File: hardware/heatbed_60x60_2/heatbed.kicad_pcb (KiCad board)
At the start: 2 copper layers, 60 x 60 mm, 1 part, among them J1 PWR

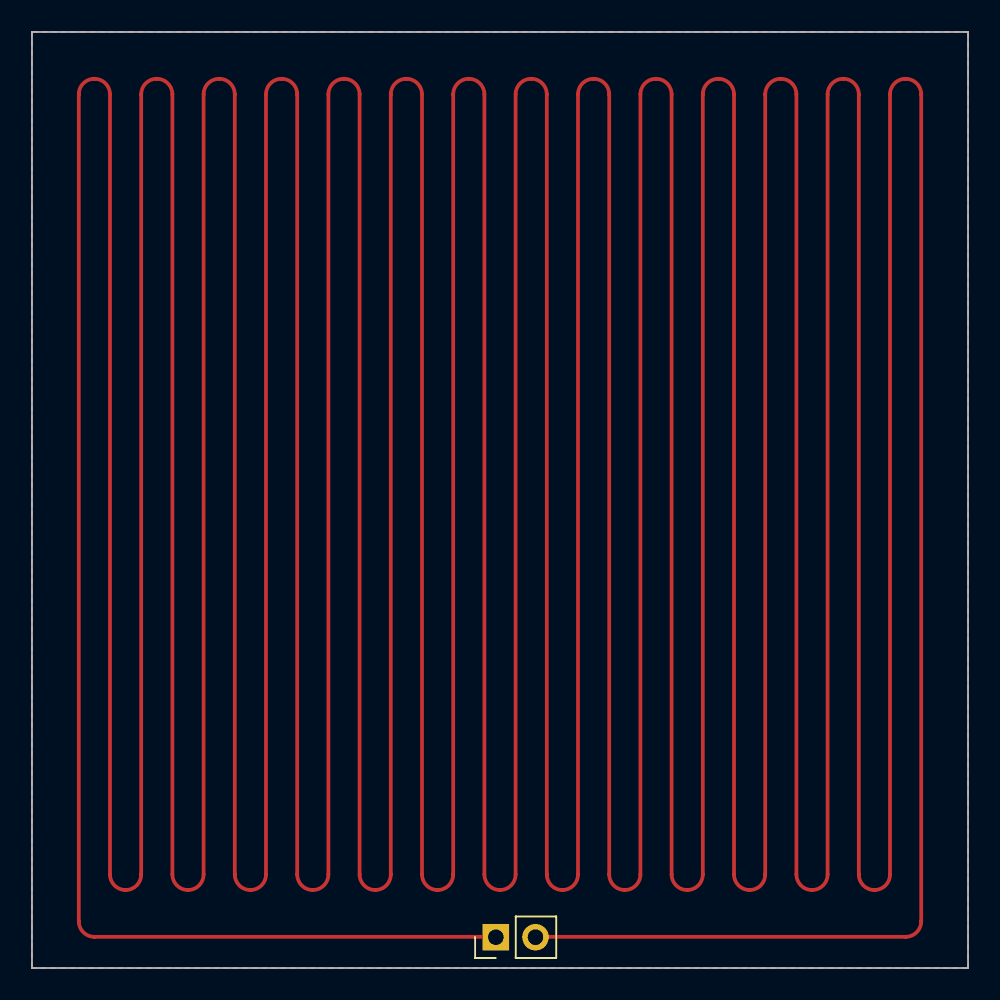
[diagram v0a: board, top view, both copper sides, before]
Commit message: Further increase tracks' widths
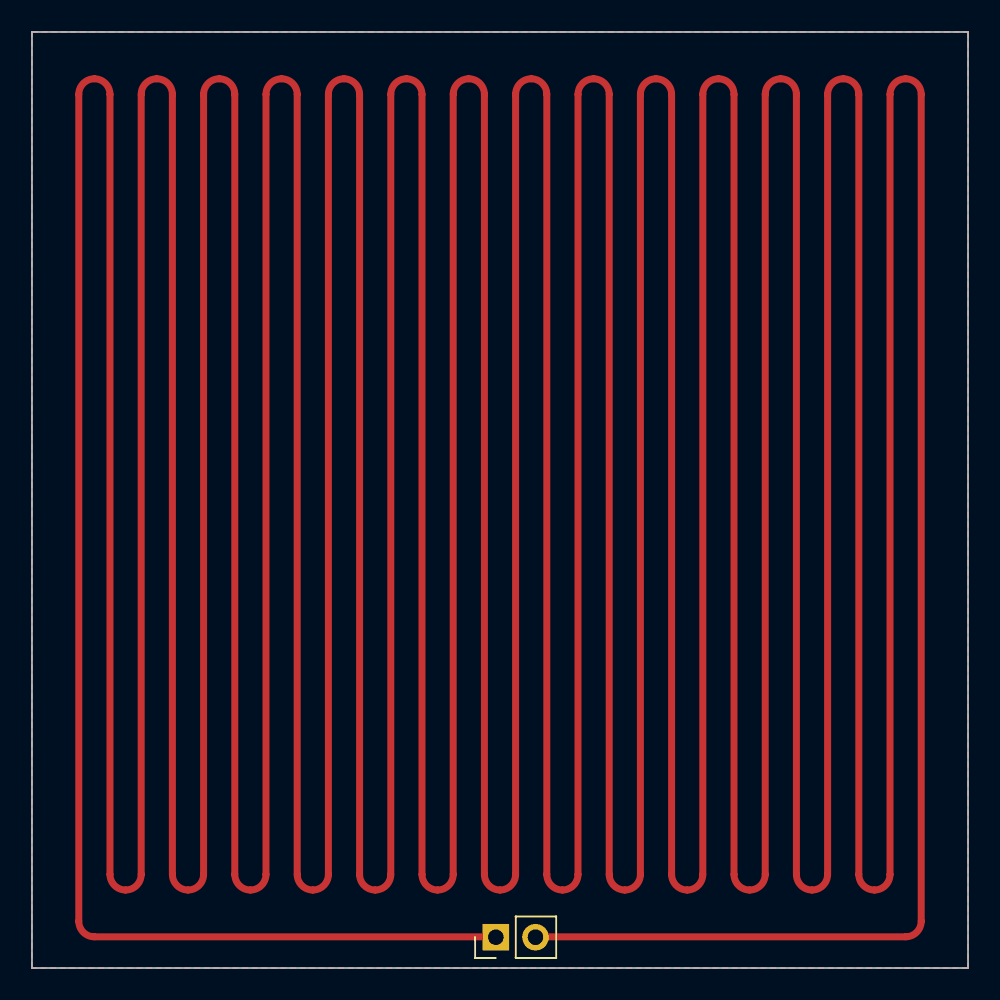
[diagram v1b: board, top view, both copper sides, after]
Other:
- board text added: "Width: 0.449 mm | Length: 1543.49 mm | Resistance: 2.97 Ω"
- board text removed: "Width: 0.241 mm | Length: 1543.49 mm | Resistance: 5.24 Ω"

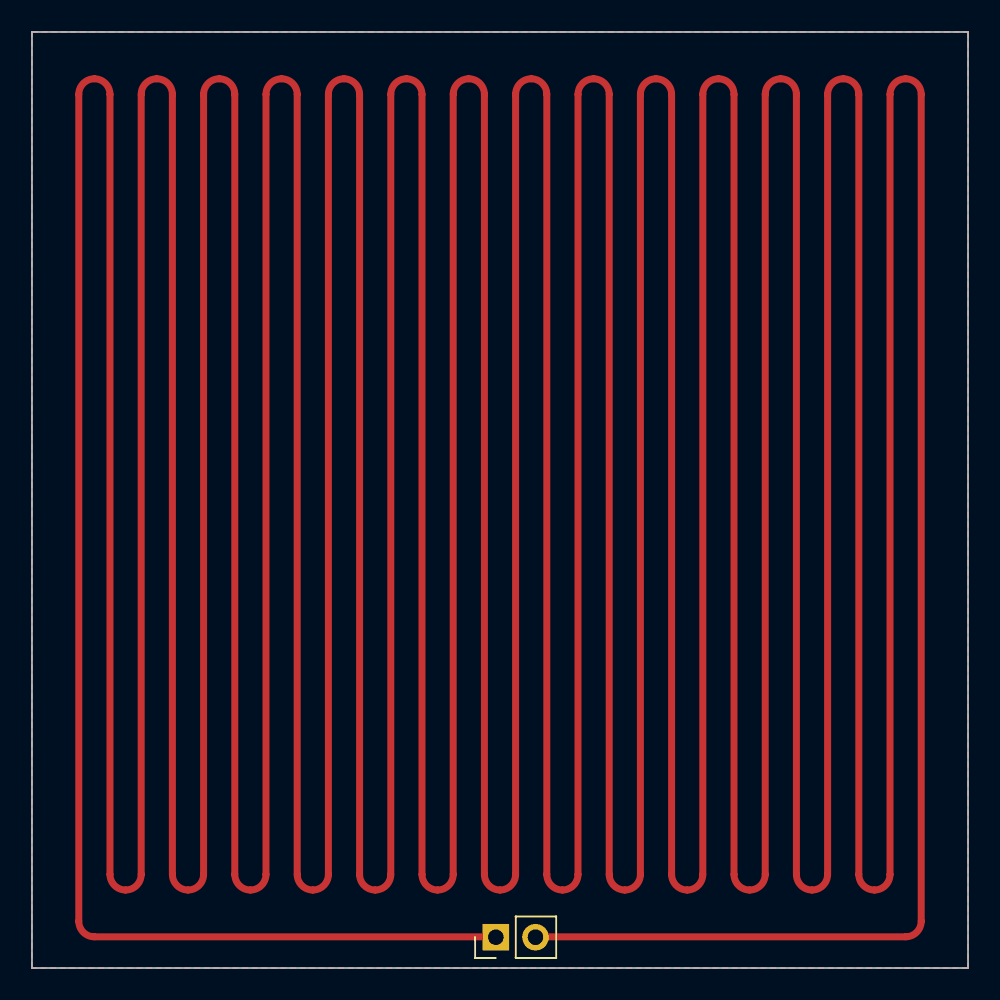
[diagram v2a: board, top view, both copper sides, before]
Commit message: Increase holes' diameters
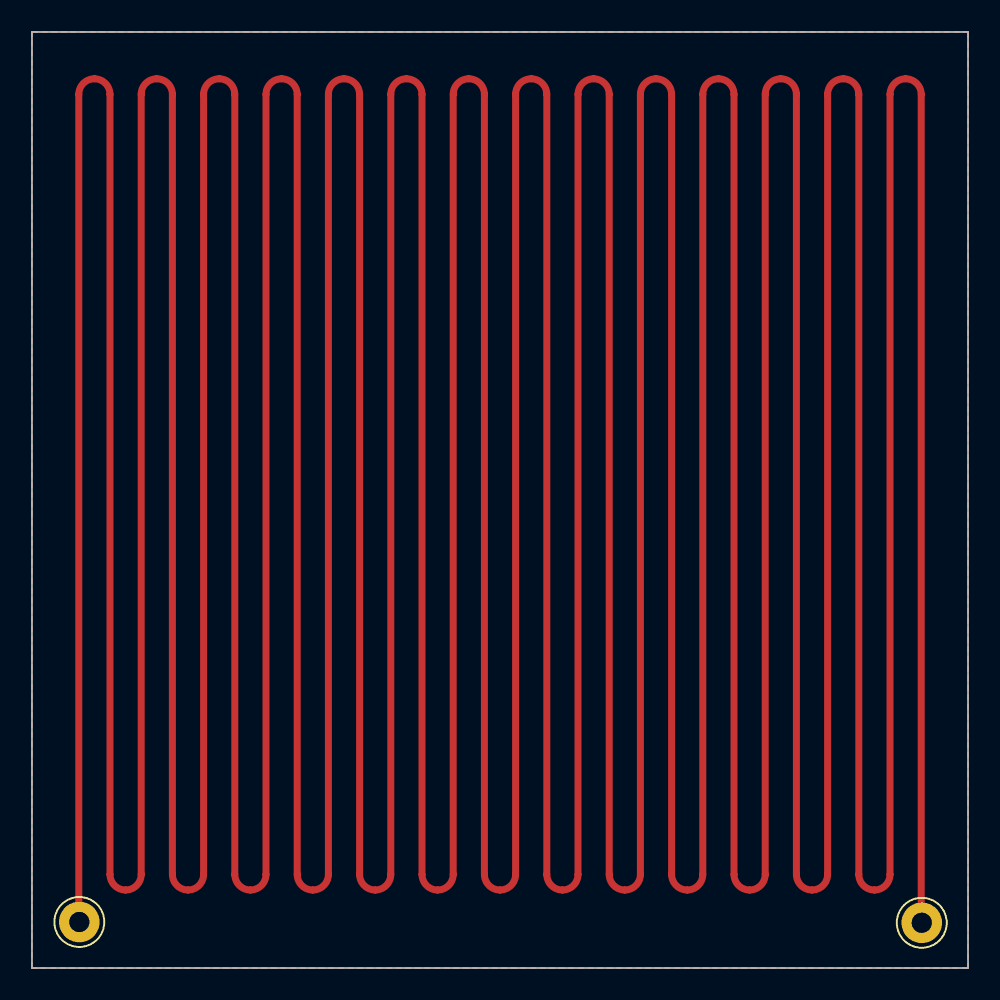
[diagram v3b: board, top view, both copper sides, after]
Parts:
- added J2: Conn_01x01, Connector_Pin:Pin_D1.3mm_L11.0mm, F.Cu at (176.0, 130.1)
- J1: value PWR -> Conn_01x01; footprint Connector_PinHeader_2.54mm:PinHeader_1x02_P2.54mm_Vertical -> Connector_Pin:Pin_D1.3mm_L11.0mm
- moved J1 26.7 mm to (122.0, 130.1), turned to 0 degrees
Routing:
- net Net-(J1-Pin_1): track 1541.3 -> 1488.8 mm
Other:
- board text removed: "Width: 0.449 mm | Length: 1543.49 mm | Resistance: 2.97 Ω"
